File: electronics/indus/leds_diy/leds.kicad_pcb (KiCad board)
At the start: 2 copper layers, 21 parts, among them P1 LED+, P2 THERM, P3 LED-

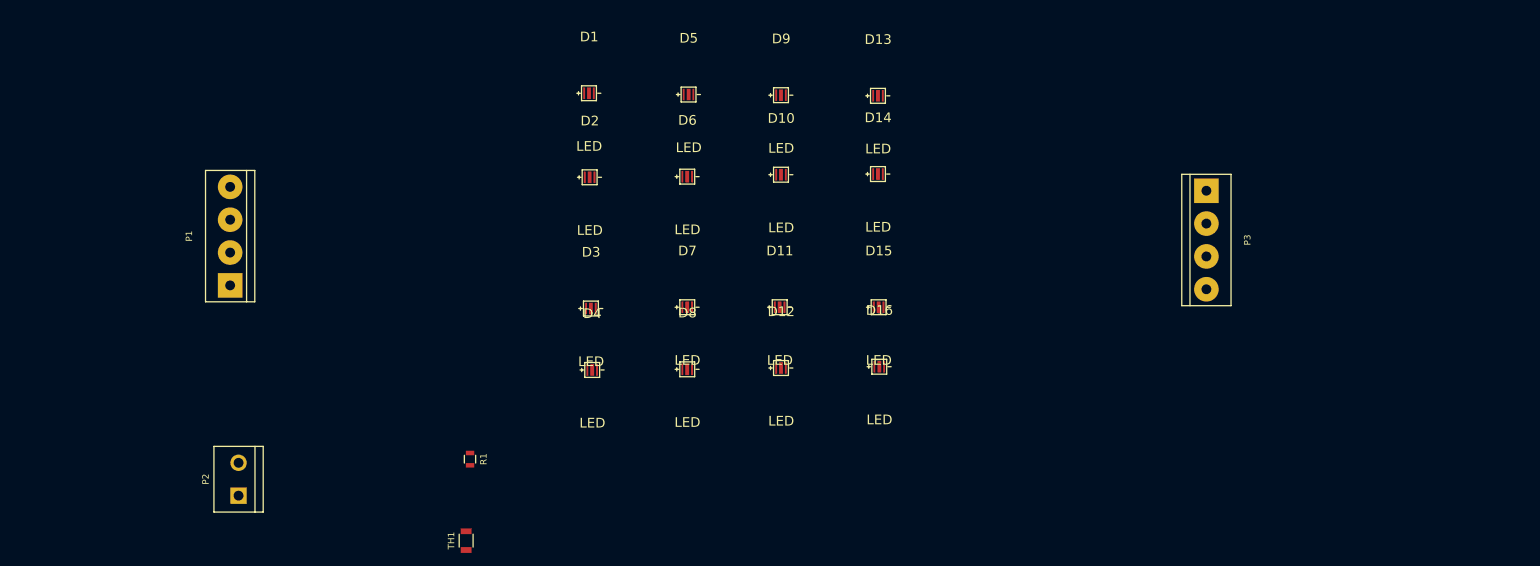
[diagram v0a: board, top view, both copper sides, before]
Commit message: first routing of led
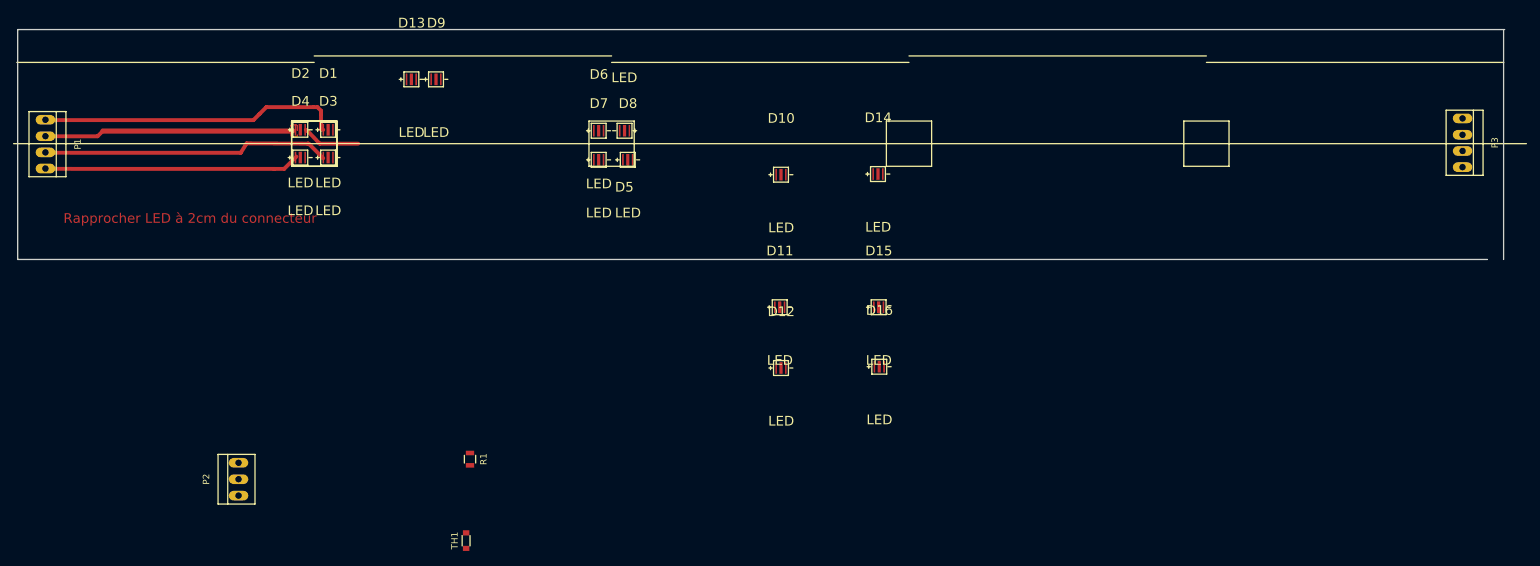
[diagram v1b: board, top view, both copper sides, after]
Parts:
- D1, D10, D11, D12, D13, D14, D15, D16, D2, D3, D4, D5, D6, D7, D8, D9: footprint Luxeon:LUXEON-C -> risebox:LUXEON-C
- P1, P3: footprint Connect:bornier4 -> risebox:PINHEAD_LOCK_1-4
- P2: footprint Connect:bornier2 -> risebox:PINHEAD_LOCK_1-3
- R1: value 10K -> 2.7K
- TH1: value THERM CTN 10K -> NTCS0603E3272JMT; footprint Resistors_SMD:R_1206 -> risebox:THERM_NTCS0603E3272JMT_SMD0603
- moved D13 72.2 mm to (101.5, 77.5)
- moved D4 55.8 mm to (84.3, 89.7)
- moved D9 53.4 mm to (105.3, 77.5)
- moved D3 46.9 mm to (88.7, 89.7)
- moved D2 45.3 mm to (84.3, 85.3)
- moved P3 42.4 mm to (264.1, 87.4)
- moved D1 40.7 mm to (88.7, 85.3)
- moved D8 33.7 mm to (135.0, 90.0)
- moved P1 31.9 mm to (44.9, 87.6), turned to 270 degrees
- moved D7 26.6 mm to (130.5, 90.0)
- moved D6 15.4 mm to (130.5, 85.5)
- moved D5 11.4 mm to (134.5, 85.5), turned to 180 degrees
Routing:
- net Net-(D2-Pad1): track 0.00 -> 72.3 mm
- net Net-(D1-Pad1): track 0.00 -> 53.6 mm
- net Net-(D4-Pad1): track 0.00 -> 34.0 mm
- net Net-(D3-Pad1): track 0.00 -> 11.9 mm
- net Net-(D2-Pad2): track 0.00 -> 9.00 mm
- added copper zone on F.Cu, net Net-(D2-Pad1)
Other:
- board outline added: 230 x 35.6 mm
- net class Default: clearance 0.254 -> 0.8; trace_width 0.254 -> 0.6
- net class pads added: clearance 0.3, trace_width 0.6, via_dia 0.889, via_drill 0.635
- rule trace_clearance: 0.254 -> 0.8
- board text added: "Rapprocher LED à 2cm du connecteur"

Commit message: led routing - one done
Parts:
- moved D1 14.7 mm to (74.0, 85.5)
- moved D2 14.7 mm to (69.7, 85.5)
- moved D3 14.7 mm to (74.0, 89.8)
- moved D4 14.7 mm to (69.7, 89.8)
- moved P1 0.30 mm to (45.2, 87.7)
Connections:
- P1 pad 1: Net-(D4-Pad1) -> Net-(D1-Pad1)
- P1 pad 2: Net-(D3-Pad1) -> Net-(D2-Pad1)
- P1 pad 3: Net-(D2-Pad1) -> Net-(D3-Pad1)
- P1 pad 4: Net-(D1-Pad1) -> Net-(D4-Pad1)
- P3 pad 1: Net-(D13-Pad2) -> Net-(D16-Pad2)
- P3 pad 2: Net-(D14-Pad2) -> Net-(D15-Pad2)
- P3 pad 3: Net-(D15-Pad2) -> Net-(D14-Pad2)
- P3 pad 4: Net-(D16-Pad2) -> Net-(D13-Pad2)
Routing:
- net Net-(D2-Pad1): track 72.3 -> 24.2 mm
- net Net-(D1-Pad1): track 53.6 -> 32.1 mm
- net Net-(D3-Pad1): track 11.9 -> 29.5 mm
- net Net-(D4-Pad1): track 34.0 -> 25.4 mm
- net Net-(D1-Pad2): track 0.00 -> 8.47 mm
- net Net-(D4-Pad2): track 0.00 -> 7.60 mm
- net Net-(D3-Pad2): track 0.00 -> 5.00 mm
- added copper zone on F.Cu, net Net-(D1-Pad2)
- added copper zone on F.Cu, net Net-(D2-Pad2)
- added copper zone on F.Cu, net Net-(D3-Pad1)
- added copper zone on F.Cu, net Net-(D3-Pad2)
- added copper zone on F.Cu, net Net-(D4-Pad1)
- added copper zone on F.Cu, net Net-(D4-Pad2)
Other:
- board text removed: "Rapprocher LED à 2cm du connecteur"

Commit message: 2 leds
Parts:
- moved D13 133.7 mm to (235.2, 80.3)
- moved D9 133.7 mm to (239.0, 80.3)
- moved D10 70.6 mm to (229.2, 96.0)
- moved D11 63.8 mm to (222.3, 112.4)
- moved D12 63.8 mm to (222.5, 121.8)
- moved D15 63.8 mm to (237.6, 112.4)
- moved D16 63.8 mm to (237.7, 121.6)
- moved D14 51.4 mm to (224.9, 96.1)
- moved D8 8.23 mm to (126.8, 89.5)
- moved D6 3.73 mm to (126.8, 85.2)
- moved D5 3.44 mm to (131.1, 85.2), turned to 0 degrees
- moved D7 0.79 mm to (131.1, 89.5)
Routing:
- net Net-(D3-Pad2): track 5.00 -> 57.8 mm
- net Net-(D1-Pad2): track 8.47 -> 60.9 mm
- net Net-(D4-Pad2): track 7.60 -> 59.2 mm
- net Net-(D2-Pad2): track 9.00 -> 57.4 mm
- net Net-(D12-Pad1): track 0.00 -> 12.9 mm
- net Net-(D10-Pad1): track 0.00 -> 12.7 mm
- net Net-(D5-Pad2): track 0.00 -> 7.43 mm
- net Net-(D11-Pad1): track 0.00 -> 6.46 mm
